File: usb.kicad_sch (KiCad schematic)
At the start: 3 parts, among them J1 USB_C_Receptacle_USB2.0

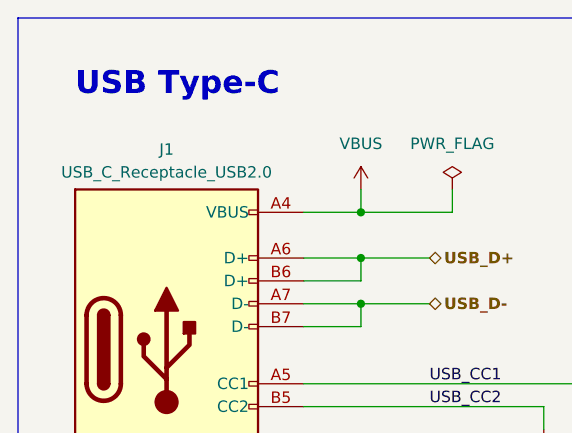
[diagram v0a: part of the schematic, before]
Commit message: Update Kicad version and remove ignored files
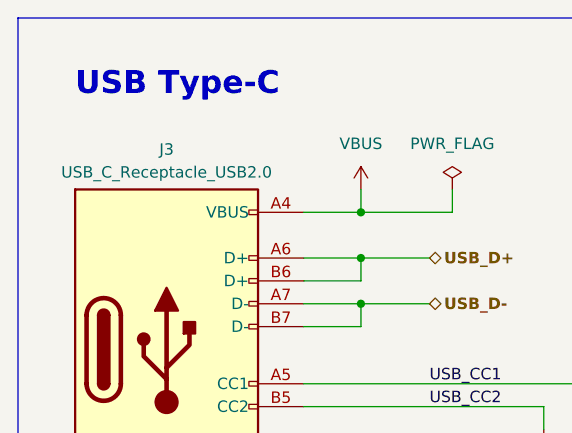
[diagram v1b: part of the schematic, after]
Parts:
- renumbered J1 to J3

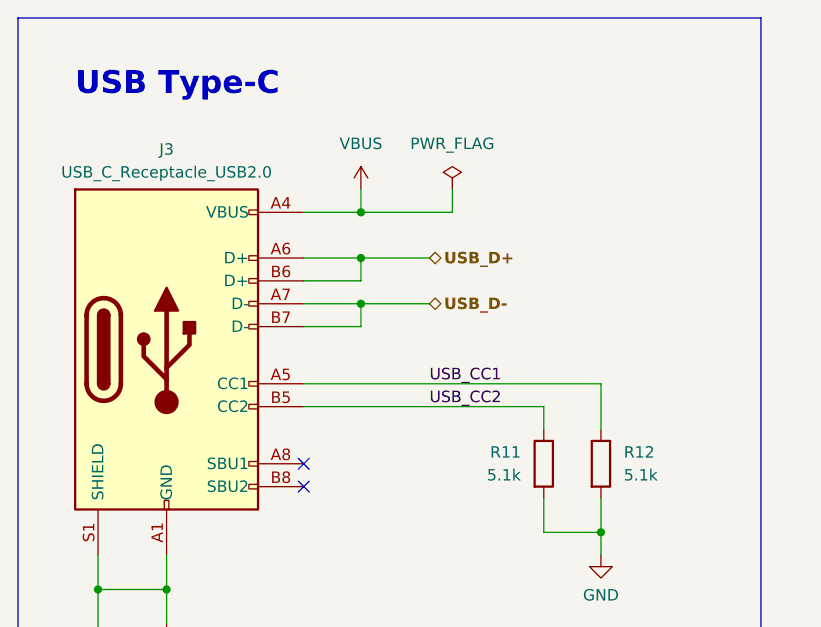
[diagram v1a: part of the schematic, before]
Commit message: break out subcircuits, add switching regulator
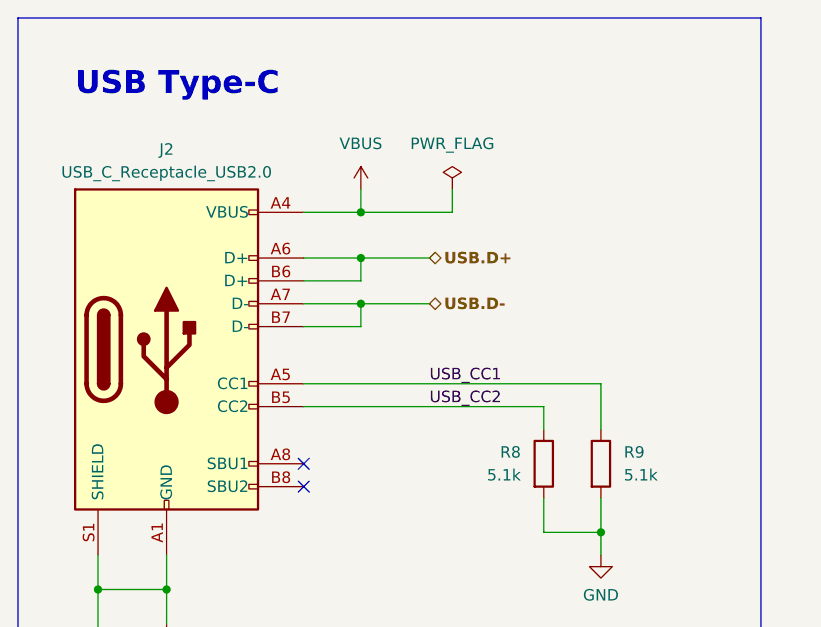
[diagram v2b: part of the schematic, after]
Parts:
- renumbered J3 to J2, R11 to R8, R12 to R9
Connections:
- net USB_D+ renamed USB.D+
- net USB_D- renamed USB.D-
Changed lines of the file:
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@@
 		)
 	)
-	(hierarchical_label "USB_D-"
+	(hierarchical_label "USB.D-"
 		(shape bidirectional)
 		(at 58.42 44.45 0)
@@
 		)
 	)
-	(hierarchical_label "USB_D+"
+	(hierarchical_label "USB.D+"
 		(shape bidirectional)
 		(at 58.42 39.37 0)
@@
 		(dnp no)
 		(fields_autoplaced yes)
-		(property "Reference" "J3"
+		(property "Reference" "J2"
 			(at 29.21 27.305 0)
 			(effects
@@
 			(project "cubesat_rp2040"
 				(path "/5511013b-c214-40ba-8960-f470f52474f8/827fa2e5-5cb5-4cf2-935c-289587867af3"
-					(reference "J3")
+					(reference "J2")
 					(unit 1)
 				)
@@
 		(dnp no)
 		(fields_autoplaced yes)
-		(property "Reference" "#PWR022"
+		(property "Reference" "#PWR023"
 			(at 50.8 35.56 0)
 			(effects
@@
 			(project "cubesat_rp2040"
 				(path "/5511013b-c214-40ba-8960-f470f52474f8/827fa2e5-5cb5-4cf2-935c-289587867af3"
-					(reference "#PWR022")
+					(reference "#PWR023")
 					(unit 1)
 				)
@@
 		(dnp no)
 		(fields_autoplaced yes)
-		(property "Reference" "#PWR023"
+		(property "Reference" "#PWR024"
 			(at 77.47 78.74 0)
 			(effects
@@
 			(project "cubesat_rp2040"
 				(path "/5511013b-c214-40ba-8960-f470f52474f8/827fa2e5-5cb5-4cf2-935c-289587867af3"
-					(reference "#PWR023")
+					(reference "#PWR024")
 					(unit 1)
 				)
@@
 		(dnp no)
 		(fields_autoplaced yes)
-		(property "Reference" "R12"
+		(property "Reference" "R9"
 			(at 80.01 60.96 0)
 			(effects
@@
 			(project "cubesat_rp2040"
 				(path "/5511013b-c214-40ba-8960-f470f52474f8/827fa2e5-5cb5-4cf2-935c-289587867af3"
-					(reference "R12")
+					(reference "R9")
 					(unit 1)
 				)
@@
 		(dnp no)
 		(fields_autoplaced yes)
-		(property "Reference" "#FLG01"
+		(property "Reference" "#FLG02"
 			(at 60.96 29.845 0)
 			(effects
@@
 			(project "cubesat_rp2040"
 				(path "/5511013b-c214-40ba-8960-f470f52474f8/827fa2e5-5cb5-4cf2-935c-289587867af3"
-					(reference "#FLG01")
+					(reference "#FLG02")
 					(unit 1)
 				)
@@
 		(dnp no)
 		(fields_autoplaced yes)
-		(property "Reference" "R11"
+		(property "Reference" "R8"
 			(at 68.58 60.96 0)
 			(effects
@@
 			(project "cubesat_rp2040"
 				(path "/5511013b-c214-40ba-8960-f470f52474f8/827fa2e5-5cb5-4cf2-935c-289587867af3"
-					(reference "R11")
+					(reference "R8")
 					(unit 1)
 				)
@@
 		(dnp no)
 		(fields_autoplaced yes)
-		(property "Reference" "#PWR024"
+		(property "Reference" "#PWR022"
 			(at 29.21 86.36 0)
 			(effects
@@
 			(project "cubesat_rp2040"
 				(path "/5511013b-c214-40ba-8960-f470f52474f8/827fa2e5-5cb5-4cf2-935c-289587867af3"
-					(reference "#PWR024")
+					(reference "#PWR022")
 					(unit 1)
 				)
@@
 		(dnp no)
 		(fields_autoplaced yes)
-		(property "Reference" "#FLG02"
+		(property "Reference" "#FLG01"
 			(at 21.59 83.185 0)
 			(effects
@@
 			(project "cubesat_rp2040"
 				(path "/5511013b-c214-40ba-8960-f470f52474f8/827fa2e5-5cb5-4cf2-935c-289587867af3"
-					(reference "#FLG02")
-					(unit 1)
-				)
+					(reference "#FLG01")
+					(unit 1)
+				)

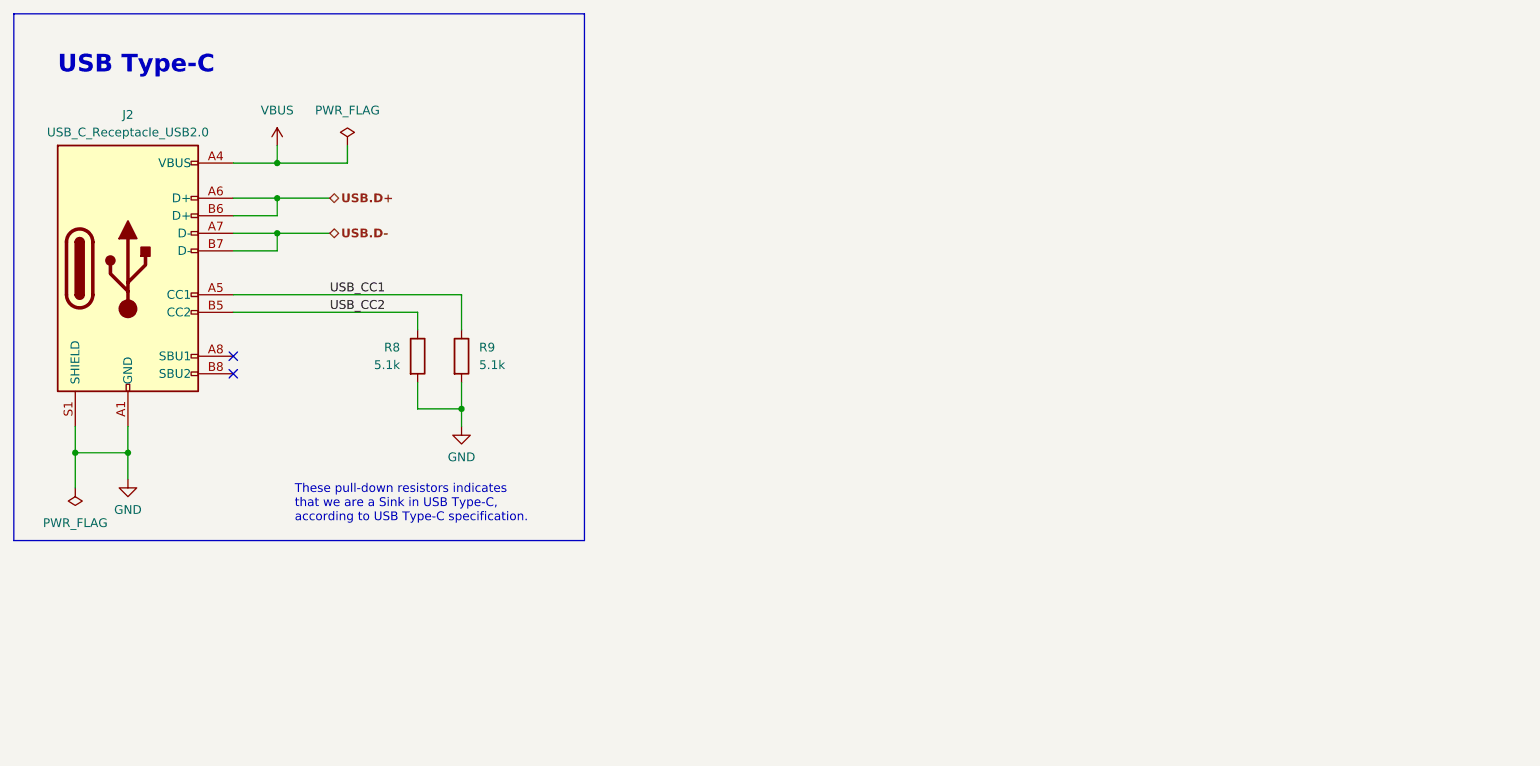
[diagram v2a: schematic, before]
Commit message: Block diagram
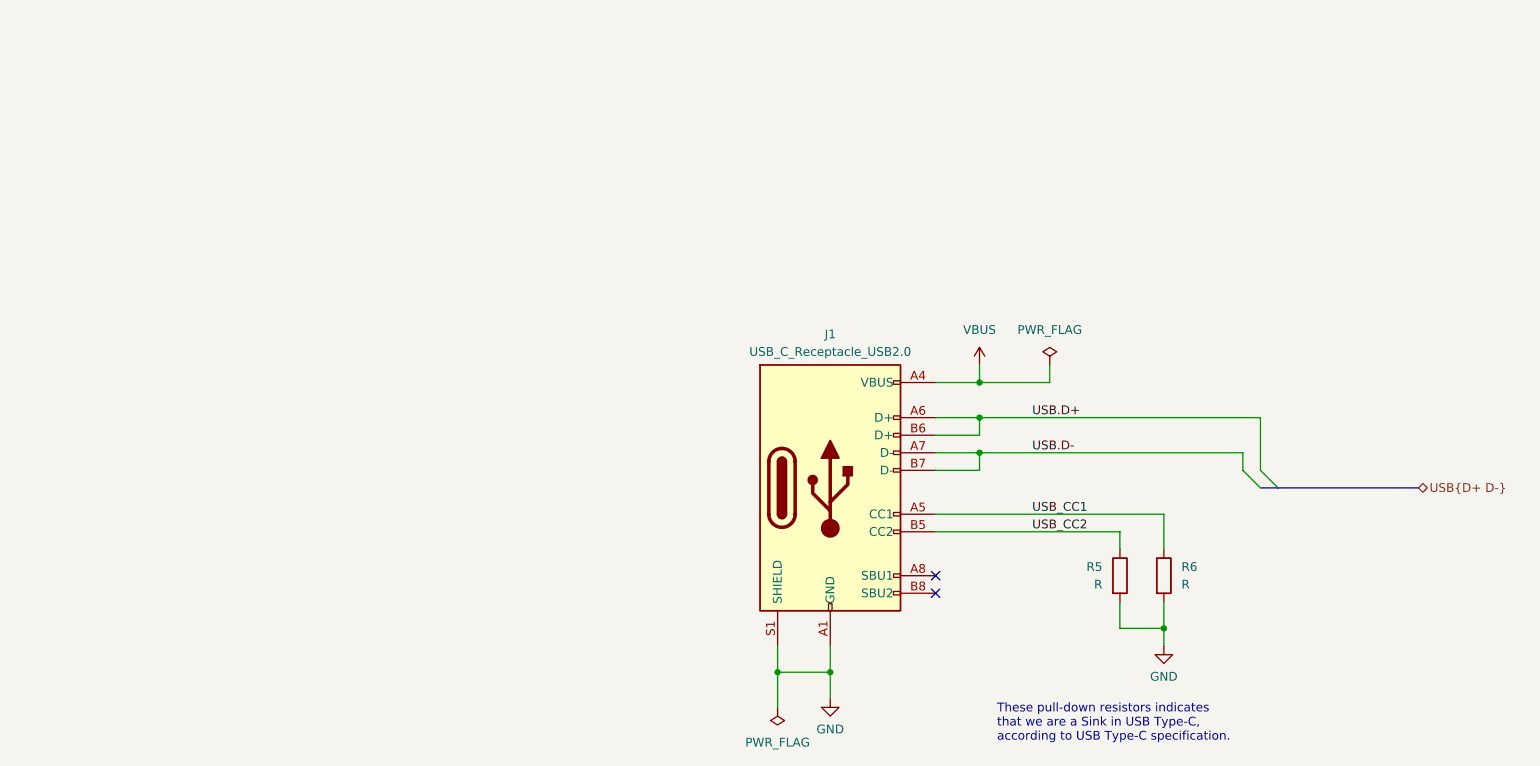
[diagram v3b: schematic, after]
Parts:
- J1: renamed from J2; footprint Connector_USB:USB_C_Receptacle_GCT_USB4105-xx-A_16P_TopMnt_Horizontal -> (none)
- R5: renamed from R8; value 5.1k -> R; footprint Resistor_SMD:R_1206_3216Metric -> Resistor_SMD:R_0402_1005Metric
- R6: renamed from R9; value 5.1k -> R; footprint Resistor_SMD:R_1206_3216Metric -> Resistor_SMD:R_0402_1005Metric
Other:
- note removed: "USB Type-C"
- moved on the sheet: J1, R5, R6

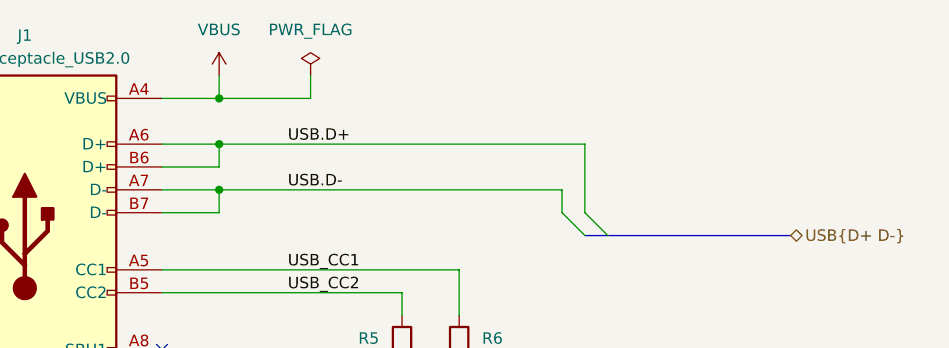
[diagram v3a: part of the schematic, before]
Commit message: Complete power regulator schematics
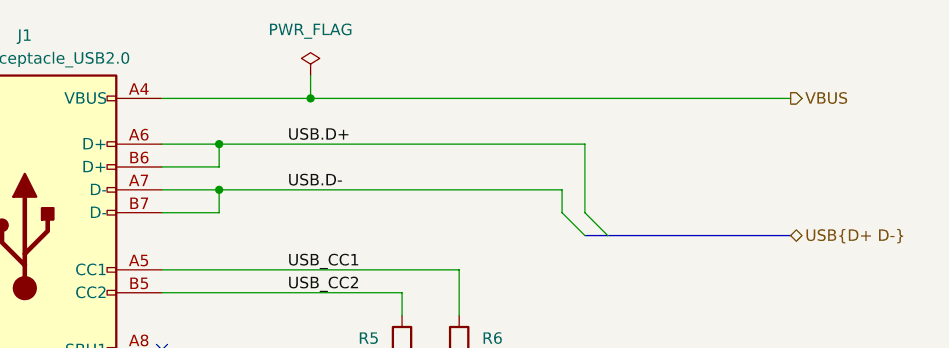
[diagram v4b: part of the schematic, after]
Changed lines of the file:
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@@
 	(paper "A4")
 	(junction
+		(at 162.56 66.04)
+		(diameter 0)
+		(color 0 0 0 0)
+	)
+	(junction
 		(at 152.4 76.2)
 		(diameter 0)
@@
 	(junction
 		(at 152.4 71.12)
-		(diameter 0)
-		(color 0 0 0 0)
-	)
-	(junction
-		(at 152.4 66.04)
 		(diameter 0)
 		(color 0 0 0 0)
@@
 	(wire
 		(pts
-			(xy 146.05 66.04) (xy 152.4 66.04)
-		)
-		(stroke
-			(width 0)
-			(type default)
-		)
-	)
-	(wire
-		(pts
 			(xy 172.72 87.63) (xy 146.05 87.63)
 		)
@@
 	(wire
 		(pts
-			(xy 152.4 66.04) (xy 162.56 66.04)
+			(xy 146.05 66.04) (xy 162.56 66.04)
 		)
 		(stroke
@@
 	(wire
 		(pts
-			(xy 152.4 66.04) (xy 152.4 63.5)
-		)
-		(stroke
-			(width 0)
-			(type default)
-		)
-	)
-	(wire
-		(pts
 			(xy 152.4 76.2) (xy 190.5 76.2)
 		)
@@
 		(pts
 			(xy 152.4 78.74) (xy 152.4 76.2)
+		)
+		(stroke
+			(width 0)
+			(type default)
+		)
+	)
+	(wire
+		(pts
+			(xy 162.56 66.04) (xy 215.9 66.04)
 		)
 		(stroke
@@
 		(shape bidirectional)
 		(at 215.9 81.28 0)
+		(fields_autoplaced yes)
+		(effects
+			(font
+				(size 1.27 1.27)
+			)
+			(justify left)
+		)
+	)
+	(hierarchical_label "VBUS"
+		(shape output)
+		(at 215.9 66.04 0)
 		(fields_autoplaced yes)
 		(effects
@@
 					(unit 1)
 				)
-			)
-		)
-	)
-	(symbol
-		(lib_id "power:VBUS")
-		(at 152.4 63.5 0)
-		(unit 1)
-		(exclude_from_sim no)
-		(in_bom yes)
-		(on_board yes)
-		(dnp no)
-		(fields_autoplaced yes)
-		(property "Reference" "#PWR013"
-			(at 152.4 67.31 0)
-			(effects
-				(font
-					(size 1.27 1.27)
-				)
-				(hide yes)
-			)
-		)
-		(property "Value" "VBUS"
-			(at 152.4 58.42 0)
-			(effects
-				(font
-					(size 1.27 1.27)
-				)
-			)
-		)
-		(property "Footprint" ""
-			(at 152.4 63.5 0)
-			(effects
-				(font
-					(size 1.27 1.27)
-				)
-				(hide yes)
-			)
-		)
-		(property "Datasheet" ""
-			(at 152.4 63.5 0)
-			(effects
-				(font
-					(size 1.27 1.27)
-				)
-				(hide yes)
-			)
-		)
-		(property "Description" "Power symbol creates a global label with name \"VBUS\""
-			(at 152.4 63.5 0)
-			(effects
-				(font
-					(size 1.27 1.27)
-				)
-				(hide yes)
-			)
-		)
-		(pin "1"
-		)
-		(instances
-			(project "cubesat_rp2040"
-				(path "/5511013b-c214-40ba-8960-f470f52474f8/827fa2e5-5cb5-4cf2-935c-289587867af3"
-					(reference "#PWR013")
-					(unit 1)
-				)

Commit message: Update footprints, route switching regulator circuit block
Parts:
- J1: footprint (none) -> Connector_USB:USB_C_Receptacle_Amphenol_12401548E4-2A
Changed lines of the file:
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@@
 			)
 		)
-		(property "Footprint" ""
+		(property "Footprint" "Connector_USB:USB_C_Receptacle_Amphenol_12401548E4-2A"
 			(at 134.62 81.28 0)
 			(effects

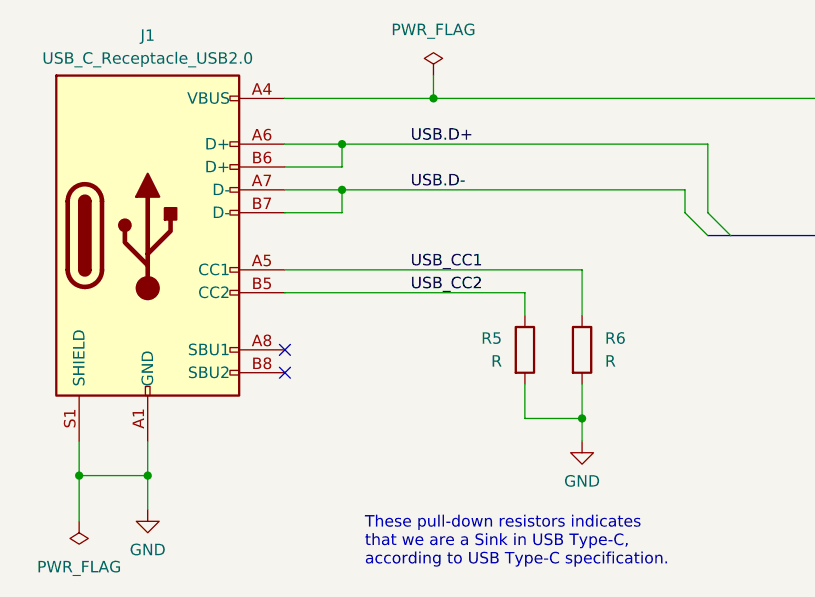
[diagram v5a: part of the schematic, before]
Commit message: Update footprints, route more circuit blocks
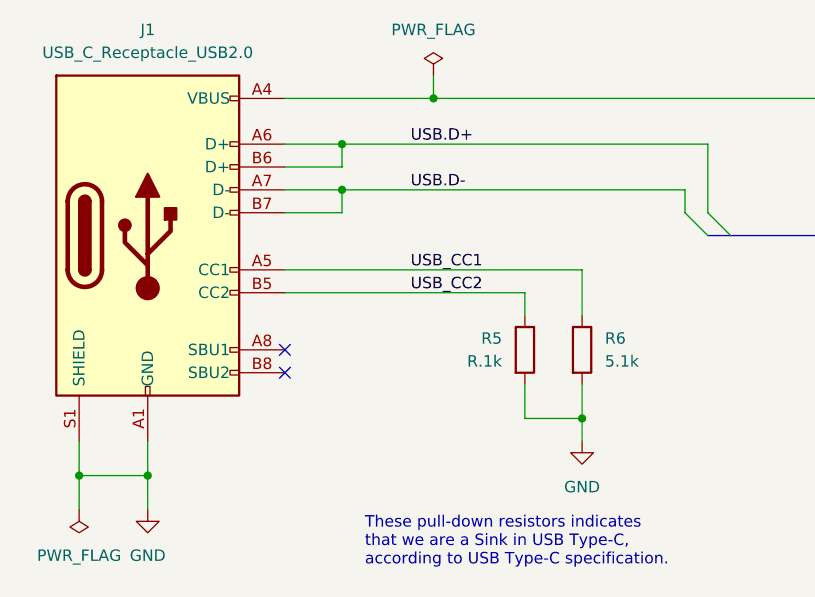
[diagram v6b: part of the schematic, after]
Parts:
- J1: footprint Connector_USB:USB_C_Receptacle_Amphenol_12401548E4-2A -> Connector_USB:USB_C_Receptacle_GCT_USB4105-xx-A_16P_TopMnt_Horizontal
- R5: value R -> R.1k
- R6: value R -> 5.1k
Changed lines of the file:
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@@
 	(wire
 		(pts
-			(xy 123.19 107.95) (xy 123.19 113.03)
+			(xy 123.19 107.95) (xy 123.19 111.76)
 		)
 		(stroke
@@
 		(fields_autoplaced yes)
 		(property "Reference" "J1"
-			(at 130.81 59.055 0)
+			(at 130.81 58.42 0)
 			(effects
 				(font
@@
 		)
 		(property "Value" "USB_C_Receptacle_USB2.0"
-			(at 130.81 61.595 0)
-			(effects
-				(font
-					(size 1.27 1.27)
-				)
-			)
-		)
-		(property "Footprint" "Connector_USB:USB_C_Receptacle_Amphenol_12401548E4-2A"
+			(at 130.81 60.96 0)
+			(effects
+				(font
+					(size 1.27 1.27)
+				)
+			)
+		)
+		(property "Footprint" "Connector_USB:USB_C_Receptacle_GCT_USB4105-xx-A_16P_TopMnt_Horizontal"
 			(at 134.62 81.28 0)
 			(effects
@@
 		)
 		(property "Value" "GND"
-			(at 179.07 108.585 0)
+			(at 179.07 109.22 0)
 			(effects
 				(font
@@
 		(fields_autoplaced yes)
 		(property "Reference" "R6"
-			(at 181.61 92.71 0)
+			(at 181.61 92.7099 0)
 			(effects
 				(font
@@
 			)
 		)
-		(property "Value" "R"
-			(at 181.61 95.25 0)
+		(property "Value" "5.1k"
+			(at 181.61 95.2499 0)
 			(effects
 				(font
@@
 		(fields_autoplaced yes)
 		(property "Reference" "R5"
-			(at 170.18 92.71 0)
+			(at 170.18 92.7099 0)
 			(effects
 				(font
@@
 			)
 		)
-		(property "Value" "R"
-			(at 170.18 95.25 0)
+		(property "Value" "R.1k"
+			(at 170.18 95.2499 0)
 			(effects
 				(font
@@
 		)
 		(property "Value" "GND"
-			(at 130.81 116.205 0)
+			(at 130.81 116.84 0)
 			(effects
 				(font
@@
 	(symbol
 		(lib_id "power:PWR_FLAG")
-		(at 123.19 113.03 180)
+		(at 123.19 111.76 180)
 		(unit 1)
 		(exclude_from_sim no)
@@
 		(fields_autoplaced yes)
 		(property "Reference" "#FLG01"
-			(at 123.19 114.935 0)
+			(at 123.19 113.665 0)
 			(effects
 				(font
@@
 		)
 		(property "Value" "PWR_FLAG"
-			(at 123.19 118.11 0)
+			(at 123.19 116.84 0)
 			(effects
 				(font
@@
 		)
 		(property "Footprint" ""
-			(at 123.19 113.03 0)
+			(at 123.19 111.76 0)
 			(effects
 				(font
@@
 		)
 		(property "Datasheet" "~"
-			(at 123.19 113.03 0)
+			(at 123.19 111.76 0)
 			(effects
 				(font
@@
 		)
 		(property "Description" "Special symbol for telling ERC where power comes from"
-			(at 123.19 113.03 0)
-			(effects
-				(font
+			(at 123.19 111.76 0)
+			(effects
+				(font

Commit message: Big update, bad commit messsage :)
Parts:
- added C301: 100n, cubesat_rp2040:C_0402_1005Metric, symbol Device:C
- added C302: 1n, cubesat_rp2040:C_0402_1005Metric, symbol Device:C
- added C303: 10u, cubesat_rp2040:C_0402_1005Metric, symbol Device:C
- added R305: 1M, cubesat_rp2040:R_0402_1005Metric, symbol Device:R
- R301: renamed from R5; value R.1k -> 5.1k 10%; footprint Resistor_SMD:R_0402_1005Metric -> cubesat_rp2040:R_0402_1005Metric
- R302: renamed from R6; value 5.1k -> 5.1k 10%; footprint Resistor_SMD:R_0402_1005Metric -> cubesat_rp2040:R_0402_1005Metric
- renumbered J1 to J301
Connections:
- net GND: now also C301.2, C302.2, C303.2, R305.2; no longer J301.S1 (SHIELD)
- net VBUS: now also C303.1
- net USB.D+ renamed USB_UP.D+
- net USB.D- renamed USB_UP.D-
- net USB_CC1 renamed USB_UP.CC1
- net USB_CC2 renamed USB_UP.CC2
- new net Earth: C301.1, C302.1, J301.S1 (SHIELD), R305.1
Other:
- company: (none) -> Magnus Oksbøl Therkelsen
- title: (none) -> CubeSat RP2040 Board
- moved on the sheet: J301, R301, R302
